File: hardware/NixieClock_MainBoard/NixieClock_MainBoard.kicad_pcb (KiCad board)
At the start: 2 copper layers, 152.4 x 63.5 mm, 68 parts, among them J1 Conn_01x14, J10 Conn_01x04, J2 Conn_01x08, J3 Conn_01x08, J4 Conn_01x08, J5 Conn_01x08, J6 USB_C_Receptacle_USB2.0_16P, J7 Micro_SD_Card, J8 Conn_01x08, J9 Conn_01x03, Q1 BC847, Q2 BC847, U1 ESP32-WROOM-32E, U10 NC7SZ125M5X, U11 NC7SZ125M5X, U12 NC7SZ125M5X, U13 NC7SZ125M5X, U14 CP2102N-Axx-xQFN24, U15 CH340C, U2 R-78C3.3-1.0, U4 PCA9635, U5 NC7SZ125M5X, U6 PCA9583A, U7 NC7SZ125M5X, U8 NC7SZ125M5X, U9 NC7SZ125M5X

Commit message: change sd card footprint changes on mainboard layout add stl files for display case
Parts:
- added H1: MountingHole, MountingHole:MountingHole_3.2mm_M3, F.Cu at (185.4, 81.3)
- added H2: MountingHole, MountingHole:MountingHole_3.2mm_M3, F.Cu at (185.4, 134.6)
- added H3: MountingHole, MountingHole:MountingHole_3.2mm_M3, F.Cu at (43.2, 134.6)
- added H4: MountingHole, MountingHole:MountingHole_3.2mm_M3, F.Cu at (43.2, 109.6)
- added H5: MountingHole, MountingHole:MountingHole_3.2mm_M3, F.Cu at (83.2, 109.5)
- added H6: MountingHole, MountingHole:MountingHole_3.2mm_M3, F.Cu at (145.4, 109.5)
- added R25: 10k, Resistor_SMD:R_0603_1608Metric, B.Cu at (63.9, 97.0)
- added R26: 10k, Resistor_SMD:R_0603_1608Metric, B.Cu at (72.4, 106.8)
- J7: footprint Connector_Card:microSD_HC_Molex_47219-2001 -> Connector_Card:microSD_HC_Hirose_DM3D-SF
- U6: value PCA9583A -> PCA9538A
- moved C5 12.4 mm to (74.0, 82.7)
- moved C6 12.4 mm to (74.0, 85.2)
- moved C4 3.58 mm to (72.2, 101.3), turned to 0 degrees
- moved C10 2.92 mm to (52.7, 95.9)
- moved C9 2.80 mm to (51.1, 95.9)
- moved C3 2.05 mm to (72.2, 103.0), turned to 0 degrees
- moved U6 0.64 mm to (53.1, 90.8), turned to 0 degrees
- moved C11 0.41 mm to (179.7, 104.0), turned to 90 degrees
- moved J7 0.25 mm to (83.1, 82.9)
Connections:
- C11 pad 1: +3.3V -> Net-(J9-Pin_1)
- U10 pad 1: unconnected-(U10-~{OE}-Pad1) -> GND
- U10 pad 3: unconnected-(U10-GND-Pad3) -> GND
- U10 pad 5: unconnected-(U10-VCC-Pad5) -> +3.3V
- U13 pad 1: +3.3V -> GND
- U13 pad 5: +3.3V -> Net-(J9-Pin_1)
- U4 pad 2: GND -> Net-(U4-A1)
- U4 pad 23: GND -> Net-(U4-~{OE})
- U4 pad 24: GND -> Net-(U4-A1)
- U4 pad 25: GND -> Net-(U4-A1)
- U4 pad 3: GND -> Net-(U4-A1)
- U4 pad 4: GND -> Net-(U4-A1)
- U4 pad 5: GND -> Net-(U4-A1)
- U5 pad 1: unconnected-(U5-~{OE}-Pad1) -> GND
- U5 pad 3: unconnected-(U5-GND-Pad3) -> GND
- U5 pad 5: unconnected-(U5-VCC-Pad5) -> +3.3V
- U6 pad 1: GND -> +3.3V
- U6 pad 10: Net-(J8-Pin_8) -> unconnected-(U6-IO0_7-Pad10)
- U6 pad 11: unconnected-(U6-IO0_6-Pad11) -> /~{INT_IO}
- U6 pad 12: unconnected-(U6-IO0_7-Pad12) -> /SCL
- U6 pad 13: /~{INT_IO} -> /SDA
- U6 pad 14: /SCL -> +3.3V
- U6 pad 15: /SDA -> GND
- U6 pad 16: +3.3V -> GND
- U6 pad 2: GND -> Net-(J8-Pin_3)
- U6 pad 3: +3.3V -> Net-(J8-Pin_4)
- U6 pad 4: Net-(J8-Pin_3) -> Net-(J8-Pin_5)
- U6 pad 5: Net-(J8-Pin_4) -> Net-(J8-Pin_6)
- U6 pad 6: Net-(J8-Pin_5) -> GND
- U6 pad 7: Net-(J8-Pin_6) -> Net-(J8-Pin_7)
- U6 pad 8: GND -> Net-(J8-Pin_8)
- U6 pad 9: Net-(J8-Pin_7) -> unconnected-(U6-IO0_6-Pad9)
- U7 pad 1: unconnected-(U7-~{OE}-Pad1) -> GND
- U7 pad 3: unconnected-(U7-GND-Pad3) -> GND
- U7 pad 5: unconnected-(U7-VCC-Pad5) -> +3.3V
- U8 pad 1: unconnected-(U8-~{OE}-Pad1) -> GND
- U8 pad 3: unconnected-(U8-GND-Pad3) -> GND
- U8 pad 5: unconnected-(U8-VCC-Pad5) -> +3.3V
- U9 pad 1: unconnected-(U9-~{OE}-Pad1) -> GND
- U9 pad 3: unconnected-(U9-GND-Pad3) -> GND
- U9 pad 5: unconnected-(U9-VCC-Pad5) -> +3.3V
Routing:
- net +3.3V: track 411.5 -> 452.0 mm, vias 8 -> 14
- net Net-(U4-A1): track 0.00 -> 16.7 mm
- net /MISO: track 44.1 -> 33.4 mm
- net GND: track 107.2 -> 99.9 mm, vias 122 -> 119
- net Net-(J9-Pin_1): track 7.57 -> 13.5 mm
- net /SCLK: track 223.1 -> 217.4 mm
- net /MOSI: track 221.7 -> 226.2 mm
- net Net-(U4-~{OE}): track 0.00 -> 3.66 mm
- net /CS_0: track 76.5 -> 73.3 mm
- net /VDD: track 153.3 -> 150.4 mm
- net /~{INT_IO}: track 93.9 -> 91.5 mm
- net /CS_MEM_1: track 42.1 -> 44.4 mm
- net /SDA: track 87.7 -> 89.2 mm
- net /SCL: track 83.9 -> 85.4 mm
- net Net-(J8-Pin_3): track 11.0 -> 9.68 mm
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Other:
- board text added: "KEEPOUT"

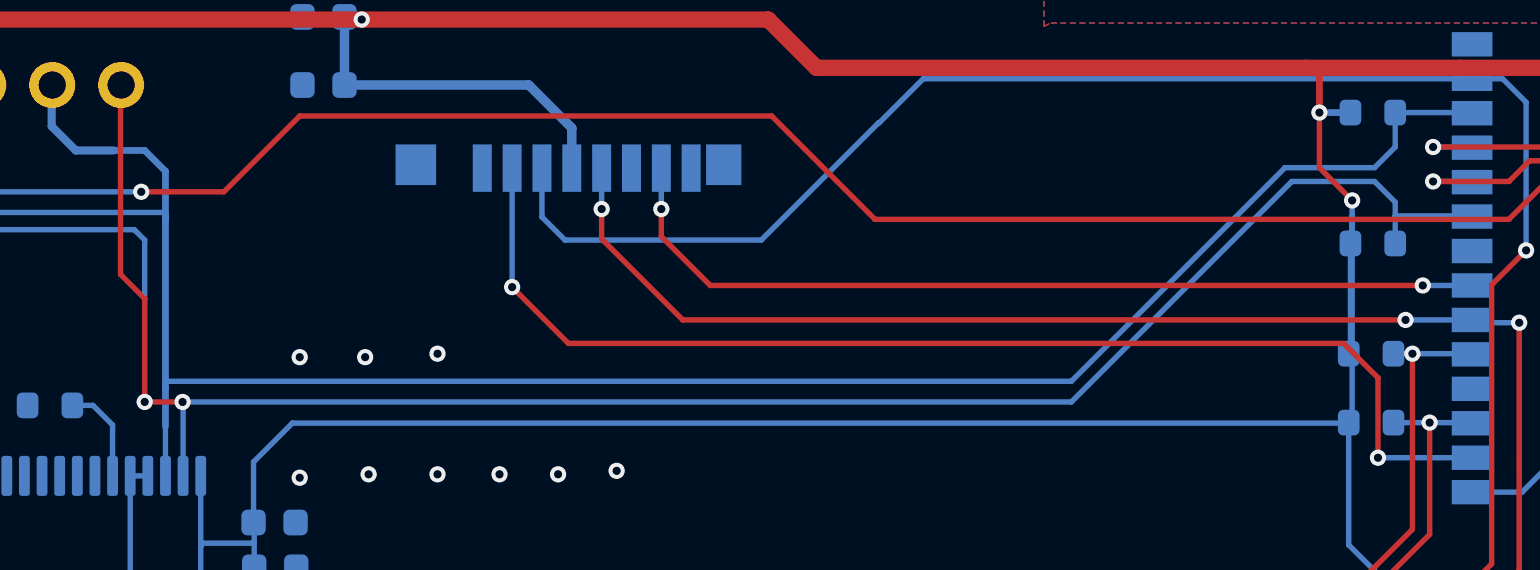
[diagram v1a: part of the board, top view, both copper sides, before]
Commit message: display 1.14 anpassungen. Stecker war verpolt
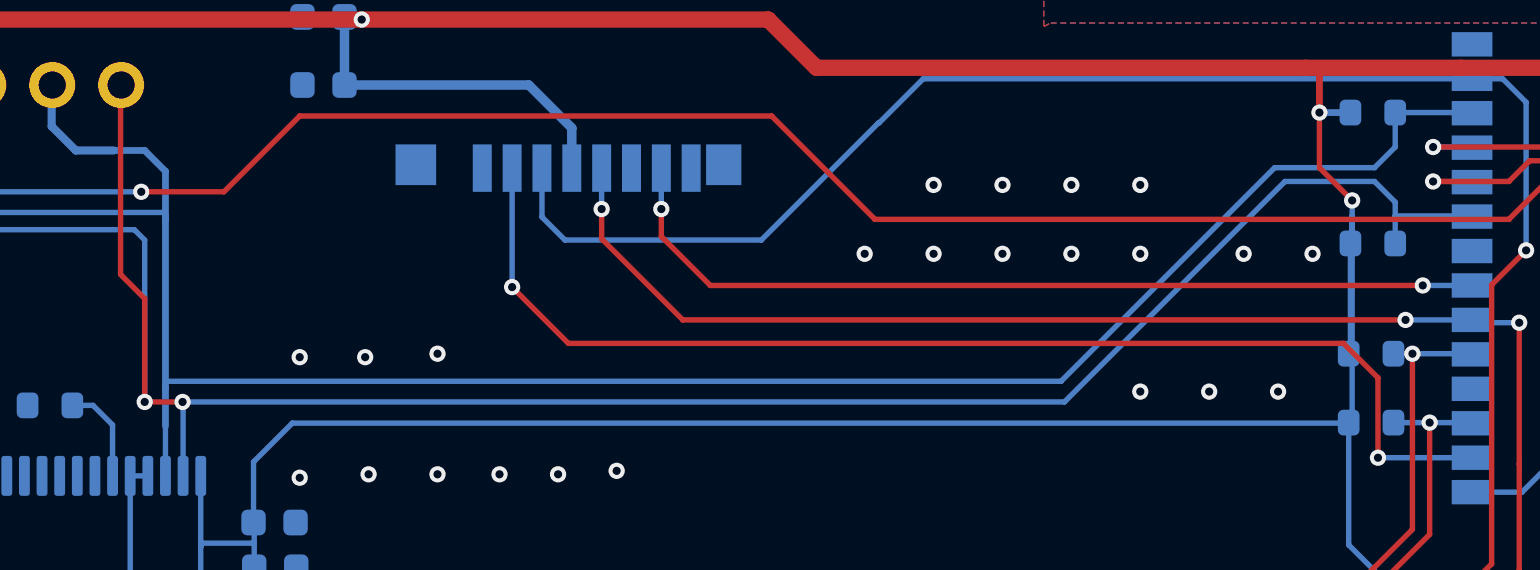
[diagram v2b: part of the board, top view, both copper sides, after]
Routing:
- net GND: vias 119 -> 133
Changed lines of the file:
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@@
 			(plot_on_all_layers_selection 0x0000000_00000000)
 			(disableapertmacros no)
-			(usegerberextensions no)
-			(usegerberattributes yes)
-			(usegerberadvancedattributes yes)
-			(creategerberjobfile yes)
+			(usegerberextensions yes)
+			(usegerberattributes no)
+			(usegerberadvancedattributes no)
+			(creategerberjobfile no)
 			(dashed_line_dash_ratio 12.000000)
 			(dashed_line_gap_ratio 3.000000)
@@
 			(psa4output no)
 			(plotreference yes)
-			(plotvalue yes)
+			(plotvalue no)
 			(plotfptext yes)
 			(plotinvisibletext no)
 			(sketchpadsonfab no)
-			(subtractmaskfromsilk no)
+			(subtractmaskfromsilk yes)
 			(outputformat 1)
 			(mirror no)
-			(drillshape 1)
+			(drillshape 0)
 			(scaleselection 1)
-			(outputdirectory "")
+			(outputdirectory "gerber/")
 		)
 	)
@@
 		(tags "resistor")
 		(property "Reference" "R5"
-			(at -3.62 0 0)
+			(at -2.477 -0.635 0)
 			(layer "B.SilkS")
 			(effects
@@
 	)
 	(via
+		(at 107.95 91.44)
+		(size 0.6)
+		(drill 0.3)
+		(layers "F.Cu" "B.Cu")
+		(free yes)
+		(net 2)
+	)
+	(via
 		(at 189.23 82.55)
 		(size 0.6)
@@
 	)
 	(via
+		(at 99.06 91.44)
+		(size 0.6)
+		(drill 0.3)
+		(layers "F.Cu" "B.Cu")
+		(free yes)
+		(net 2)
+	)
+	(via
 		(at 130.81 102.87)
 		(size 0.6)
@@
 	)
 	(via
+		(at 104.14 91.44)
+		(size 0.6)
+		(drill 0.3)
+		(layers "F.Cu" "B.Cu")
+		(free yes)
+		(net 2)
+	)
+	(via
 		(at 39.243 123.19)
 		(size 0.6)
@@
 	)
 	(via
+		(at 104.14 96.52)
+		(size 0.6)
+		(drill 0.3)
+		(layers "F.Cu" "B.Cu")
+		(free yes)
+		(net 2)
+	)
+	(via
 		(at 189.23 120.65)
 		(size 0.6)
@@
 	)
 	(via
+		(at 110.49 91.44)
+		(size 0.6)
+		(drill 0.3)
+		(layers "F.Cu" "B.Cu")
+		(free yes)
+		(net 2)
+	)
+	(via
 		(at 39.37 82.677)
 		(size 0.6)
@@
 	)
 	(via
+		(at 101.6 91.44)
+		(size 0.6)
+		(drill 0.3)
+		(layers "F.Cu" "B.Cu")
+		(free yes)
+		(net 2)
+	)
+	(via
 		(at 59.944 108.458)
 		(size 0.6)
@@
 	)
 	(via
+		(at 106.68 96.52)
+		(size 0.6)
+		(drill 0.3)
+		(layers "F.Cu" "B.Cu")
+		(free yes)
+		(net 2)
+	)
+	(via
 		(at 153.67 77.47)
 		(size 0.6)
@@
 	)
 	(via
+		(at 104.14 88.9)
+		(size 0.6)
+		(drill 0.3)
+		(layers "F.Cu" "B.Cu")
+		(free yes)
+		(net 2)
+	)
+	(via
 		(at 59.309 113.792)
 		(size 0.6)
@@
 	)
 	(via
+		(at 101.6 88.9)
+		(size 0.6)
+		(drill 0.3)
+		(layers "F.Cu" "B.Cu")
+		(free yes)
+		(net 2)
+	)
+	(via
 		(at 78.232 99.568)
 		(size 0.6)
@@
 	)
 	(via
+		(at 96.52 88.9)
+		(size 0.6)
+		(drill 0.3)
+		(layers "F.Cu" "B.Cu")
+		(free yes)
+		(net 2)
+	)
+	(via
 		(at 173.99 77.47)
 		(size 0.6)
@@
 	)
 	(via
+		(at 109.22 96.52)
+		(size 0.6)
+		(drill 0.3)
+		(layers "F.Cu" "B.Cu")
+		(free yes)
+		(net 2)
+	)
+	(via
 		(at 73.152 99.695)
 		(size 0.6)
@@
 	)
 	(via
+		(at 93.98 91.44)
+		(size 0.6)
+		(drill 0.3)
+		(layers "F.Cu" "B.Cu")
+		(free yes)
+		(net 2)
+	)
+	(via
 		(at 184.15 138.43)
 		(size 0.6)
@@
 	)
 	(via
+		(at 99.06 88.9)
+		(size 0.6)
+		(drill 0.3)
+		(layers "F.Cu" "B.Cu")
+		(free yes)
+		(net 2)
+	)
+	(via
 		(at 137.16 90.17)
 		(size 0.6)
@@
 		(net 2)
 	)
+	(via
+		(at 96.52 91.44)
+		(size 0.6)
+		(drill 0.3)
+		(layers "F.Cu" "B.Cu")
+		(free yes)
+		(net 2)
+	)
 	(segment
 		(start 179.832 102.743)
@@
 	)
 	(segment
-		(start 68.203 96.139)
-		(end 68.203 96.393)
+		(start 113.538 86.233)
+		(end 113.538 87.503)
+		(width 0.2)
+		(layer "B.Cu")
+		(net 70)
+	)
+	(segment
+		(start 112.776 88.265)
+		(end 109.093 88.265)
 		(width 0.2)
 		(layer "B.Cu")
@@
 	)
 	(segment
+		(start 101.219 96.139)
+		(end 68.203 96.139)
+		(width 0.2)
+		(layer "B.Cu")
+		(net 70)
+	)
+	(segment
 		(start 55.638 91.555)
 		(end 57.277 89.916)
@@
 	)
 	(segment
+		(start 109.093 88.265)
+		(end 101.219 96.139)
+		(width 0.2)
+		(layer "B.Cu")
+		(net 70)
+	)
+	(segment
 		(start 68.203 90.043)
 		(end 68.203 88.396)
@@
 	)
 	(segment
+		(start 113.538 87.503)
+		(end 112.776 88.265)
+		(width 0.2)
+		(layer "B.Cu")
+		(net 70)
+	)
+	(segment
 		(start 68.203 88.396)
 		(end 67.437 87.63)
@@
 	)
 	(segment
-		(start 101.6 96.139)
-		(end 68.203 96.139)
-		(width 0.2)
-		(layer "B.Cu")
-		(net 70)
-	)
-	(segment
 		(start 116.348 86.233)
 		(end 116.372 86.257)
@@
 	)
 	(segment
-		(start 112.776 88.265)
-		(end 109.474 88.265)
-		(width 0.2)
-		(layer "B.Cu")
-		(net 70)
-	)
-	(segment
-		(start 113.538 87.503)
-		(end 112.776 88.265)
-		(width 0.2)
-		(layer "B.Cu")
-		(net 70)
-	)
-	(segment
 		(start 57.277 89.916)
 		(end 68.203 89.916)
@@
 	)
 	(segment
-		(start 109.474 88.265)
-		(end 101.6 96.139)
-		(width 0.2)
-		(layer "B.Cu")
-		(net 70)
-	)
-	(segment
-		(start 113.538 86.233)
-		(end 113.538 87.503)
+		(start 68.203 96.139)
+		(end 68.203 96.393)
 		(width 0.2)
 		(layer "B.Cu")
@@
 	)
 	(segment
-		(start 113.538 90.043)
-		(end 113.538 89.535)
+		(start 116.348 90.043)
+		(end 116.372 90.067)
 		(width 0.2)
 		(layer "B.Cu")
@@
 	)
 	(segment
-		(start 116.348 90.043)
-		(end 116.372 90.067)
-		(width 0.2)
-		(layer "B.Cu")
-		(net 74)
-	)
-	(segment
-		(start 112.776 88.773)
-		(end 109.728 88.773)
+		(start 109.474 88.773)
+		(end 101.346 96.901)
 		(width 0.2)
 		(layer "B.Cu")
@@
 	)
 	(segment
-		(start 109.728 88.773)
-		(end 101.6 96.901)
+		(start 112.776 88.773)
+		(end 109.474 88.773)
 		(width 0.2)
 		(layer "B.Cu")
@@
 	)
 	(segment
-		(start 101.6 96.901)
-		(end 68.853 96.901)
-		(width 0.2)
-		(layer "B.Cu")
-		(net 74)
-	)
-	(segment
 		(start 113.538 89.535)
 		(end 112.776 88.773)
@@
 	)
 	(segment
+		(start 113.538 90.043)
+		(end 113.538 89.535)
+		(width 0.2)
+		(layer "B.Cu")
+		(net 74)
+	)
+	(segment
 		(start 53.836 92.2425)
 		(end 55.7125 92.2425)
@@
 		(width 0.2)
 		(layer "B.Cu")
+		(net 74)
+	)
+	(segment
+		(start 101.346 96.901)
+		(end 68.853 96.901)
+		(width 0.2)
+		(layer "B.Cu")

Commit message: V2.0 release fertig.
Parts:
- removed U11: NC7SZ125M5X, Package_TO_SOT_SMD:SOT-23-5
- added C18: 100nF, Capacitor_SMD:C_0603_1608Metric, B.Cu at (64.4, 129.0)
- added C19: 100nF, Capacitor_SMD:C_0603_1608Metric, B.Cu at (91.9, 129.0)
- added C20: 100nF, Capacitor_SMD:C_0603_1608Metric, B.Cu at (119.5, 129.2)
- added C21: 100nF, Capacitor_SMD:C_0603_1608Metric, B.Cu at (146.9, 129.0)
- added C22: 100nF, Capacitor_SMD:C_0603_1608Metric, B.Cu at (179.3, 129.1)
- added C23: 100nF, Capacitor_SMD:C_0603_1608Metric, B.Cu at (91.3, 91.4)
- added C24: 1u0, Capacitor_SMD:C_0603_1608Metric, B.Cu at (54.7, 117.6)
- added C25: 1u0, Capacitor_SMD:C_0603_1608Metric, B.Cu at (61.0, 118.9)
- added C26: 1u0, Capacitor_SMD:C_0603_1608Metric, B.Cu at (64.3, 118.9)
- added C27: 1u0, Capacitor_SMD:C_0603_1608Metric, B.Cu at (67.8, 118.9)
- added C28: 1u0, Capacitor_SMD:C_0603_1608Metric, B.Cu at (71.1, 118.9)
- added H7: MountingHole, MountingHole:MountingHole_3.2mm_M3, F.Cu at (43.2, 81.3)
- added J11: Conn_01x04, Connector_PinHeader_2.54mm:PinHeader_1x04_P2.54mm_Vertical_SMD_Pin1Left, B.Cu at (146.8, 97.4)
- added J12: Conn_01x03, Connector_PinHeader_2.54mm:PinHeader_1x03_P2.54mm_Vertical, B.Cu at (133.1, 109.7)
- added J13: Conn_01x03, Connector_PinHeader_2.54mm:PinHeader_1x04_P2.54mm_Vertical, B.Cu at (133.3, 116.0)
- added Q3: Si4532DY, Package_SO:SOIC-8_3.9x4.9mm_P1.27mm, B.Cu at (170.2, 108.5)
- added R27: 10k, Resistor_SMD:R_0603_1608Metric, B.Cu at (140.8, 101.6)
- added R28: 10k, Resistor_SMD:R_0603_1608Metric, B.Cu at (142.5, 101.6)
- added R29: 10k, Resistor_SMD:R_0603_1608Metric, B.Cu at (148.8, 89.4)
- added R30: 10k, Resistor_SMD:R_0603_1608Metric, B.Cu at (148.8, 90.9)
- added R31: 10k, Resistor_SMD:R_0603_1608Metric, B.Cu at (112.6, 100.1)
- added R32: 10k, Resistor_SMD:R_0603_1608Metric, B.Cu at (138.5, 100.8)
- added R33: 10k, Resistor_SMD:R_0603_1608Metric, B.Cu at (166.4, 104.4)
- added R34: 10k, Resistor_SMD:R_0603_1608Metric, B.Cu at (169.2, 113.4)
- added U16: NC7SZ125M5X, Package_TO_SOT_SMD:SOT-23-5, B.Cu at (89.4, 129.7)
- added U17: NC7SZ125M5X, Package_TO_SOT_SMD:SOT-23-5, B.Cu at (117.0, 129.8)
- added U18: NC7SZ125M5X, Package_TO_SOT_SMD:SOT-23-5, B.Cu at (144.4, 129.7)
- added U19: NC7SZ125M5X, Package_TO_SOT_SMD:SOT-23-5, B.Cu at (176.7, 129.7)
- added U20: NC7SZ125M5X, Package_TO_SOT_SMD:SOT-23-5, B.Cu at (95.0, 80.1)
- added U21: NC7SZ125M5X, Package_TO_SOT_SMD:SOT-23-5, B.Cu at (92.3, 87.5)
- added U3: NC7SZ125M5X, Package_TO_SOT_SMD:SOT-23-5, B.Cu at (61.8, 129.7)
- R13, R14, R15, R16, R17, R18, R19, R20, R7, R8: value 10k -> 10R
- R21: value 10k -> 0R0
- moved R9 25.9 mm to (138.4, 97.4), turned to 180 degrees
- moved R11 22.7 mm to (137.4, 92.6), turned to 180 degrees
- moved J8 5.08 mm to (43.2, 104.1)
- moved R21 1.60 mm to (178.4, 123.7)
- moved J7 1.02 mm to (82.9, 83.9), turned to 0 degrees
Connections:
- J1 pad 8: /MOSI -> /MOSI_4
- J2 pad 5: /MOSI -> /MOSI_0
- J3 pad 5: /MOSI -> /MOSI_1
- J4 pad 5: /MOSI -> /MOSI_2
- J5 pad 5: /MOSI -> /MOSI_3
- J7 pad 3: /MOSI -> Net-(J7-CMD)
- J7 pad 7: /MISO -> Net-(J7-DAT0)
- R20 pad 1: /A0 -> /DC
- U1 pad 12: /WS28XX -> /CS_0
- U1 pad 14: unconnected-(U1-IO12-Pad14) -> Net-(U1-IO12)
- U1 pad 24: /CS_2 -> unconnected-(U1-IO2-Pad24)
- U1 pad 29: /CS_0 -> unconnected-(U1-IO5-Pad29)
- U1 pad 4: unconnected-(U1-SENSOR_VP-Pad4) -> /uC/ADC_0
- U1 pad 5: unconnected-(U1-SENSOR_VN-Pad5) -> /uC/ADC_3
- U1 pad 7: unconnected-(U1-IO35-Pad7) -> /uC/WakeUp_2
- U1 pad 8: /uC/WakeUp_1 -> /CS_2
- U1 pad 9: /uC/WakeUp_2 -> /WS28XX
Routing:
- net /DC: track 0.00 -> 99.0 mm, vias 0 -> 2
- net GND: track 99.9 -> 138.7 mm, vias 133 -> 152
- net +3.3V: track 452.0 -> 489.6 mm, vias 14 -> 17
- net /uC/ADC_0: track 0.00 -> 33.7 mm, vias 0 -> 1
- net /uC/ADC_3: track 0.00 -> 32.7 mm, vias 0 -> 1
- net /VDD: track 150.4 -> 181.9 mm, vias 5 -> 6
- net /CS_2: track 25.9 -> 56.8 mm, vias 1 -> 2
- net /CS_0: track 73.3 -> 101.5 mm, vias 1 -> 2
- net /SCLK: track 217.4 -> 243.9 mm
- net /RS: track 122.2 -> 145.1 mm, vias 2 -> 9
- net /CS_MEM_1: track 44.4 -> 66.9 mm, vias 2 -> 4
- net /uC/WakeUp_2: track 0.00 -> 21.1 mm, vias 0 -> 1
- net Net-(J7-DAT0): track 0.00 -> 19.4 mm
- net /MOSI: track 226.2 -> 206.9 mm, vias 6 -> 10
- net Net-(J7-CMD): track 0.00 -> 12.0 mm
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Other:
- board text added: "- S +"
- board text added: "1 LED 2 GND 3 RES 4 RS 5 SDA 6 SCL 7 VDD 8 CS"
- board text added: "1 NC 2 GND 3 LED- 4 LED+ 5 GND 6 /RESET 7 A0 8 SDA 9 SCL 10 VCC 11 IOVCC 12 CS 13 GND 14 NC"
- board text added: "3V3 VCC 5V0"
- board text added: "A3 A0 - +"
- board text added: "EN GND GND IO0"
- board text added: "G L V"
- board text added: "IO5 IO4 IO3 IO2 IO1 IO0 GND VCC"
- board text added: "VCC GND SCL SDA"

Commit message: Version 2 Ready
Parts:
- added Q4: Si2319CDS, Package_TO_SOT_SMD:SOT-23, B.Cu at (169.3, 110.0)
- Q3: value Si4532DY -> BSS123; footprint Package_SO:SOIC-8_3.9x4.9mm_P1.27mm -> Package_TO_SOT_SMD:SOT-23
- R28, R30: value 10k -> 470R
- moved R34 6.25 mm to (172.0, 107.8), turned to 90 degrees
- moved Q3 2.57 mm to (169.3, 106.0)
- moved R33 0.99 mm to (165.7, 103.6), turned to 180 degrees
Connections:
- Q3 pad 1: GND -> /DISP_POWER_EN
- Q3 pad 2: /DISP_POWER_EN -> GND
- Q3 pad 3: +3.3V -> Net-(Q3-D)
- R34 pad 2: Net-(Q3B-G) -> Net-(Q3-D)
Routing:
- net +3.3V: track 489.6 -> 479.3 mm
- net Net-(Q3B-G): track 10.3 -> 0.00 mm
- net /VDD: track 181.9 -> 176.1 mm
- net Net-(Q3-D): track 0.00 -> 5.45 mm
- net /DISP_POWER_EN: track 55.2 -> 53.3 mm
